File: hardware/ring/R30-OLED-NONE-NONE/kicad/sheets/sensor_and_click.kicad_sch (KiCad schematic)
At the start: 0 parts

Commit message: feat(hardware): scaffold 30deg optical ring sensor/click and usb interfaces for accessibility pointing, ~$9 ring BOM
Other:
- note added: "Sensor and click interface scaffold: optical SPI, motion interrupt, and dome-click nets are locked here before the PAW3204 symbol and dome footprint land."
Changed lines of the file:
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@@
   (generator_version "0.1")
   (paper "A4")
+  (text "Sensor and click interface scaffold: optical SPI, motion interrupt, and dome-click nets are locked here before the PAW3204 symbol and dome footprint land."
+    (at 20.32 20.32 0)
+    (effects (font (size 1.27 1.27)))
+  )
+  (hierarchical_label "VREG_3V3"
+    (shape input)
+    (at 25.4 38.1 0)
+    (effects (font (size 1.27 1.27)))
+  )
+  (hierarchical_label "SENSOR_SCLK"
+    (shape input)
+    (at 25.4 45.72 0)
+    (effects (font (size 1.27 1.27)))
+  )
+  (hierarchical_label "SENSOR_NRESET"
+    (shape input)
+    (at 25.4 53.34 0)
+    (effects (font (size 1.27 1.27)))
+  )
+  (hierarchical_label "SENSOR_SDIO"
+    (shape bidirectional)
+    (at 187.96 38.1 180)
+    (effects (font (size 1.27 1.27)))
+  )
+  (hierarchical_label "SENSOR_MOTION_N"
+    (shape output)
+    (at 187.96 45.72 180)
+    (effects (font (size 1.27 1.27)))
+  )
+  (hierarchical_label "CLICK_PRIMARY_N"
+    (shape output)
+    (at 187.96 53.34 180)
+    (effects (font (size 1.27 1.27)))
+  )
   (sheet_instances
     (path "/" (page "1"))

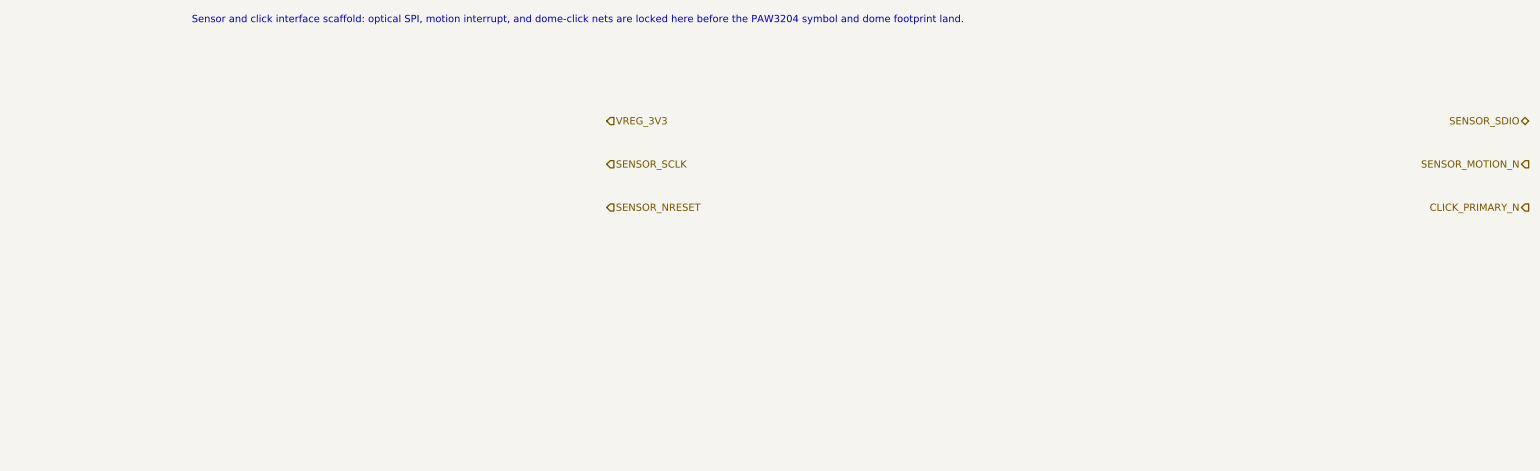
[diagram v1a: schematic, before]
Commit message: feat(hardware): lock R30 sense and schematic baseline
Design disclosure: sensing mechanism PAW3204-class optical tracking; form factor R30-OLED-NONE-NONE fingertip ring, active 30-degree ring packet; intended use BLE HID pointing for accessibility; BOM estimate ~$5.30-9.45.

Record the accepted 2N7002 charge-gate path, R7-R11 sense/status values, current KiCad red baseline, and directly linked packet truth docs.
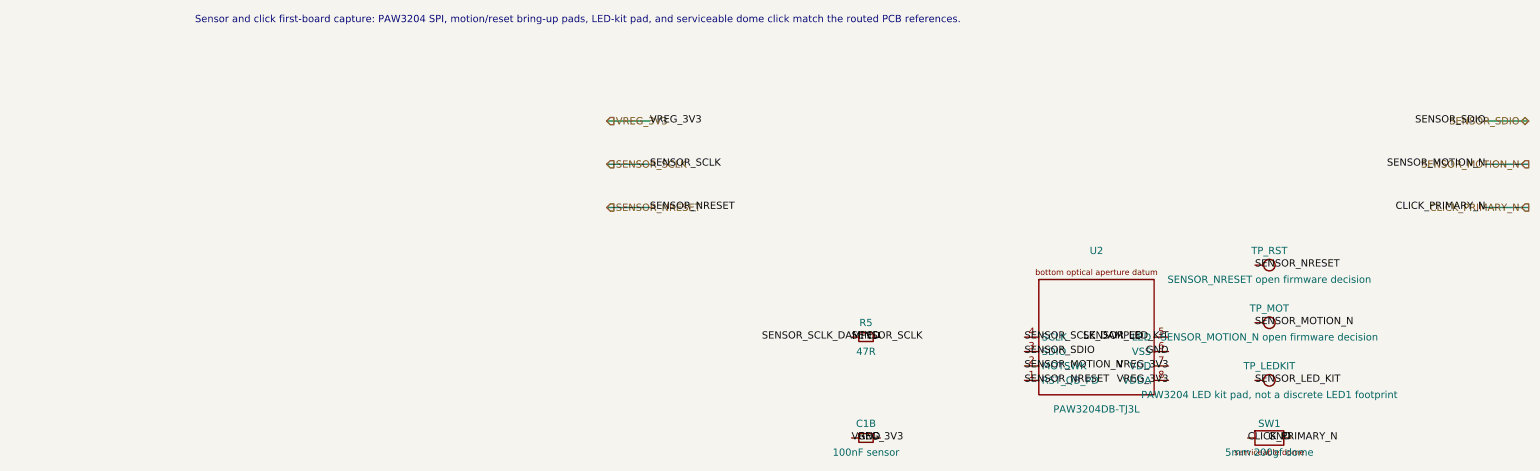
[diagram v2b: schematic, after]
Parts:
- added C1B: 100nF sensor, Capacitor_SMD:C_0402_1005Metric, symbol PowerFinger:C_0402_SUPPORT
- added R5: 47R, Resistor_SMD:R_0402_1005Metric, symbol PowerFinger:R_0402_SUPPORT
- added SW1: 5mm 200gf dome, PowerFinger_Ring:Snap_Dome_5mm_TwoPad_Serviceable, symbol PowerFinger:SNAP_DOME_2PAD
- added TP_LEDKIT: PAW3204 LED kit pad, not a discrete LED1 footprint, TestPoint:TestPoint_Pad_D1.0mm, symbol PowerFinger:TESTPAD_1MM
- added TP_MOT: SENSOR_MOTION_N open firmware decision, TestPoint:TestPoint_Pad_D1.0mm, symbol PowerFinger:TESTPAD_1MM
- added TP_RST: SENSOR_NRESET open firmware decision, TestPoint:TestPoint_Pad_D1.0mm, symbol PowerFinger:TESTPAD_1MM
- added U2: PAW3204DB-TJ3L, PowerFinger_Ring:PAW3204DB_TJ3L_Staggered_DIP8_Bottom_ApertureDatum, symbol PowerFinger:PAW3204DB-TJ3L_FirstBoard
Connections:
- net CLICK_PRIMARY_N: now also SW1.1 (CENTER)
- net SENSOR_MOTION_N: now also TP_MOT.1 (TP), U2.2 (MOTSWK)
- net SENSOR_NRESET: now also TP_RST.1 (TP), U2.1 (RST_QB_PD)
- net SENSOR_SCLK: now also R5.1
- net SENSOR_SDIO: now also U2.3 (SDIO)
- net VREG_3V3: now also C1B.1, U2.7 (VDD), U2.8 (VDDA)
- new net GND: C1B.2, SW1.2 (RING), U2.6 (VSS)
- new net SENSOR_LED_KIT: TP_LEDKIT.1 (TP), U2.5 (LED)
- new net SENSOR_SCLK_DAMPED: R5.2, U2.4 (SCLK)
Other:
- note added: "Sensor and click first-board capture: PAW3204 SPI, motion/reset bring-up pads, LED-kit pad, and serviceable dome click match the routed PCB references."
- note removed: "Sensor and click interface scaffold: optical SPI, motion interrupt, and dome-click nets are locked here before the PAW3204 symbol and dome footprint land."
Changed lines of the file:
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@@
   (generator_version "0.1")
   (paper "A4")
-  (text "Sensor and click interface scaffold: optical SPI, motion interrupt, and dome-click nets are locked here before the PAW3204 symbol and dome footprint land."
+  (text "Sensor and click first-board capture: PAW3204 SPI, motion/reset bring-up pads, LED-kit pad, and serviceable dome click match the routed PCB references."
     (at 20.32 20.32 0)
     (effects (font (size 1.27 1.27)))
   )
-  (hierarchical_label "VREG_3V3"
-    (shape input)
-    (at 25.4 38.1 0)
+  (hierarchical_label "VREG_3V3" (shape input) (at 25.4 38.1 0)
     (effects (font (size 1.27 1.27)))
   )
-  (hierarchical_label "SENSOR_SCLK"
-    (shape input)
-    (at 25.4 45.72 0)
+  (hierarchical_label "SENSOR_SCLK" (shape input) (at 25.4 45.72 0)
     (effects (font (size 1.27 1.27)))
   )
-  (hierarchical_label "SENSOR_NRESET"
-    (shape input)
-    (at 25.4 53.34 0)
+  (hierarchical_label "SENSOR_NRESET" (shape input) (at 25.4 53.34 0)
     (effects (font (size 1.27 1.27)))
   )
-  (hierarchical_label "SENSOR_SDIO"
-    (shape bidirectional)
-    (at 187.96 38.1 180)
+  (hierarchical_label "SENSOR_SDIO" (shape bidirectional) (at 187.96 38.1 180)
     (effects (font (size 1.27 1.27)))
   )
-  (hierarchical_label "SENSOR_MOTION_N"
-    (shape output)
-    (at 187.96 45.72 180)
+  (hierarchical_label "SENSOR_MOTION_N" (shape output) (at 187.96 45.72 180)
     (effects (font (size 1.27 1.27)))
   )
-  (hierarchical_label "CLICK_PRIMARY_N"
-    (shape output)
-    (at 187.96 53.34 180)
+  (hierarchical_label "CLICK_PRIMARY_N" (shape output) (at 187.96 53.34 180)
     (effects (font (size 1.27 1.27)))
   )
+  (wire (pts (xy 25.4 38.1) (xy 33.02 38.1)) (stroke (width 0) (type default) (color 0 0 0 0)))
+  (wire (pts (xy 25.4 45.72) (xy 33.02 45.72)) (stroke (width 0) (type default) (color 0 0 0 0)))
+  (wire (pts (xy 25.4 53.34) (xy 33.02 53.34)) (stroke (width 0) (type default) (color 0 0 0 0)))
+  (wire (pts (xy 180.34 38.1) (xy 187.96 38.1)) (stroke (width 0) (type default) (color 0 0 0 0)))
+  (wire (pts (xy 180.34 45.72) (xy 187.96 45.72)) (stroke (width 0) (type default) (color 0 0 0 0)))
+  (wire (pts (xy 180.34 53.34) (xy 187.96 53.34)) (stroke (width 0) (type default) (color 0 0 0 0)))
+  (label "VREG_3V3" (at 33.02 38.1 0) (effects (font (size 1.27 1.27))))
+  (label "SENSOR_SCLK" (at 33.02 45.72 0) (effects (font (size 1.27 1.27))))
+  (label "SENSOR_NRESET" (at 33.02 53.34 0) (effects (font (size 1.27 1.27))))
+  (label "SENSOR_SDIO" (at 180.34 38.1 180) (effects (font (size 1.27 1.27))))
+  (label "SENSOR_MOTION_N" (at 180.34 45.72 180) (effects (font (size 1.27 1.27))))
+  (label "CLICK_PRIMARY_N" (at 180.34 53.34 180) (effects (font (size 1.27 1.27))))
+  (symbol (lib_id "PowerFinger:PAW3204DB-TJ3L_FirstBoard") (at 111.76 76.2 0) (unit 1)
+    (in_bom yes) (on_board yes) (dnp no)
+    (property "Reference" "U2" (at 111.76 60.96 0)
+      (effects (font (size 1.27 1.27)))
+    )
+    (property "Value" "PAW3204DB-TJ3L" (at 111.76 88.9 0)
+      (effects (font (size 1.27 1.27)))
+    )
+    (property "Footprint" "PowerFinger_Ring:PAW3204DB_TJ3L_Staggered_DIP8_Bottom_ApertureDatum" (at 111.76 91.44 0)
+      (effects (font (size 1.27 1.27)) hide)
+    )
+    (property "Datasheet" "" (at 111.76 93.98 0)
+      (effects (font (size 1.27 1.27)) hide)
+    )
+    (pin "1")
+    (pin "2")
+    (pin "3")
+    (pin "4")
+    (pin "5")
+    (pin "6")
+    (pin "7")
+    (pin "8")
+    (instances
+      (project "r30_oled_none_none"
+        (path "/" (reference "U2") (unit 1))
+      )
+    )
+  )
+  (symbol (lib_id "PowerFinger:R_0402_SUPPORT") (at 71.12 76.2 0) (unit 1)
+    (in_bom yes) (on_board yes) (dnp no)
+    (property "Reference" "R5" (at 71.12 73.66 0)
+      (effects (font (size 1.27 1.27)))
+    )
+    (property "Value" "47R" (at 71.12 78.74 0)
+      (effects (font (size 1.27 1.27)))
+    )
+    (property "Footprint" "Resistor_SMD:R_0402_1005Metric" (at 71.12 81.28 0)
+      (effects (font (size 1.27 1.27)) hide)
+    )
+    (pin "1")
+    (pin "2")
+    (instances
+      (project "r30_oled_none_none"
+        (path "/" (reference "R5") (unit 1))
+      )
+    )
+  )
+  (symbol (lib_id "PowerFinger:C_0402_SUPPORT") (at 71.12 93.98 0) (unit 1)
+    (in_bom yes) (on_board yes) (dnp no)
+    (property "Reference" "C1B" (at 71.12 91.44 0)
+      (effects (font (size 1.27 1.27)))
+    )
+    (property "Value" "100nF sensor" (at 71.12 96.52 0)
+      (effects (font (size 1.27 1.27)))
+    )
+    (property "Footprint" "Capacitor_SMD:C_0402_1005Metric" (at 71.12 99.06 0)
+      (effects (font (size 1.27 1.27)) hide)
+    )
+    (property "Datasheet" "" (at 71.12 101.6 0)
+      (effects (font (size 1.27 1.27)) hide)
+    )
+    (pin "1")
+    (pin "2")
+    (instances
+      (project "r30_oled_none_none"
+        (path "/" (reference "C1B") (unit 1))
+      )
+    )
+  )
+  (symbol (lib_id "PowerFinger:SNAP_DOME_2PAD") (at 142.24 93.98 0) (unit 1)
+    (in_bom yes) (on_board yes) (dnp no)
+    (property "Reference" "SW1" (at 142.24 91.44 0)
+      (effects (font (size 1.27 1.27)))
+    )
+    (property "Value" "5mm 200gf dome" (at 142.24 96.52 0)
+      (effects (font (size 1.27 1.27)))
+    )
+    (property "Footprint" "PowerFinger_Ring:Snap_Dome_5mm_TwoPad_Serviceable" (at 142.24 99.06 0)
+      (effects (font (size 1.27 1.27)) hide)
+    )
+    (pin "1")
+    (pin "2")
+    (instances
+      (project "r30_oled_none_none"
+        (path "/" (reference "SW1") (unit 1))
+      )
+    )
+  )
+  (symbol (lib_id "PowerFinger:TESTPAD_1MM") (at 142.24 63.5 0) (unit 1)
+    (in_bom yes) (on_board yes) (dnp no)
+    (property "Reference" "TP_RST" (at 142.24 60.96 0)
+      (effects (font (size 1.27 1.27)))
+    )
+    (property "Value" "SENSOR_NRESET open firmware decision" (at 142.24 66.04 0)
+      (effects (font (size 1.27 1.27)))
+    )
+    (property "Footprint" "TestPoint:TestPoint_Pad_D1.0mm" (at 142.24 68.58 0)
+      (effects (font (size 1.27 1.27)) hide)
+    )
+    (pin "1")
+    (instances
+      (project "r30_oled_none_none"
+        (path "/" (reference "TP_RST") (unit 1))
+      )
+    )
+  )
+  (symbol (lib_id "PowerFinger:TESTPAD_1MM") (at 142.24 73.66 0) (unit 1)
+    (in_bom yes) (on_board yes) (dnp no)
+    (property "Reference" "TP_MOT" (at 142.24 71.12 0)
+      (effects (font (size 1.27 1.27)))
+    )
+    (property "Value" "SENSOR_MOTION_N open firmware decision" (at 142.24 76.2 0)
+      (effects (font (size 1.27 1.27)))
+    )
+    (property "Footprint" "TestPoint:TestPoint_Pad_D1.0mm" (at 142.24 78.74 0)
+      (effects (font (size 1.27 1.27)) hide)
+    )
+    (pin "1")
+    (instances
+      (project "r30_oled_none_none"
+        (path "/" (reference "TP_MOT") (unit 1))
+      )
+    )
+  )
+  (symbol (lib_id "PowerFinger:TESTPAD_1MM") (at 142.24 83.82 0) (unit 1)
+    (in_bom yes) (on_board yes) (dnp no)
+    (property "Reference" "TP_LEDKIT" (at 142.24 81.28 0)
+      (effects (font (size 1.27 1.27)))
+    )
+    (property "Value" "PAW3204 LED kit pad, not a discrete LED1 footprint" (at 142.24 86.36 0)
+      (effects (font (size 1.27 1.27)))
+    )
+    (property "Footprint" "TestPoint:TestPoint_Pad_D1.0mm" (at 142.24 88.9 0)
+      (effects (font (size 1.27 1.27)) hide)
+    )
+    (pin "1")
+    (instances
+      (project "r30_oled_none_none"
+        (path "/" (reference "TP_LEDKIT") (unit 1))
+      )
+    )
+  )
+  (label "SENSOR_NRESET" (at 99.06 83.82 0) (effects (font (size 1.27 1.27))))
+  (label "SENSOR_MOTION_N" (at 99.06 81.28 0) (effects (font (size 1.27 1.27))))
+  (label "SENSOR_SDIO" (at 99.06 78.74 0) (effects (font (size 1.27 1.27))))
+  (label "SENSOR_SCLK_DAMPED" (at 99.06 76.2 0) (effects (font (size 1.27 1.27))))
+  (label "SENSOR_LED_KIT" (at 124.46 76.2 180) (effects (font (size 1.27 1.27))))
+  (label "GND" (at 124.46 78.74 180) (effects (font (size 1.27 1.27))))
+  (label "VREG_3V3" (at 124.46 81.28 180) (effects (font (size 1.27 1.27))))
+  (label "VREG_3V3" (at 124.46 83.82 180) (effects (font (size 1.27 1.27))))
+  (label "SENSOR_SCLK" (at 68.58 76.2 0) (effects (font (size 1.27 1.27))))
+  (label "SENSOR_SCLK_DAMPED" (at 73.66 76.2 180) (effects (font (size 1.27 1.27))))
+  (label "VREG_3V3" (at 68.58 93.98 0) (effects (font (size 1.27 1.27))))
+  (label "GND" (at 73.66 93.98 180) (effects (font (size 1.27 1.27))))
+  (label "CLICK_PRIMARY_N" (at 138.43 93.98 0) (effects (font (size 1.27 1.27))))
+  (label "GND" (at 146.05 93.98 180) (effects (font (size 1.27 1.27))))
+  (label "SENSOR_NRESET" (at 139.7 63.5 0) (effects (font (size 1.27 1.27))))
+  (label "SENSOR_MOTION_N" (at 139.7 73.66 0) (effects (font (size 1.27 1.27))))
+  (label "SENSOR_LED_KIT" (at 139.7 83.82 0) (effects (font (size 1.27 1.27))))
   (sheet_instances
     (path "/" (page "1"))

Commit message: fix(r30): clean schematic erc library baseline
Design disclosure: sensing mechanism PAW3204-class optical tracking; form factor R30-OLED-NONE-NONE fingertip ring, active 30-degree ring packet; intended use BLE HID pointing for accessibility; BOM estimate ~$5.30-9.45.

Materialize the project-local PowerFinger symbol and PowerFinger_Ring footprint libraries, wire sheet-interface labels, keep PAW3204 reset/motion local to sensor test pads, and update the verified KiCad snapshot to ERC=0, DRC=349, unconnected=41, parity=118.
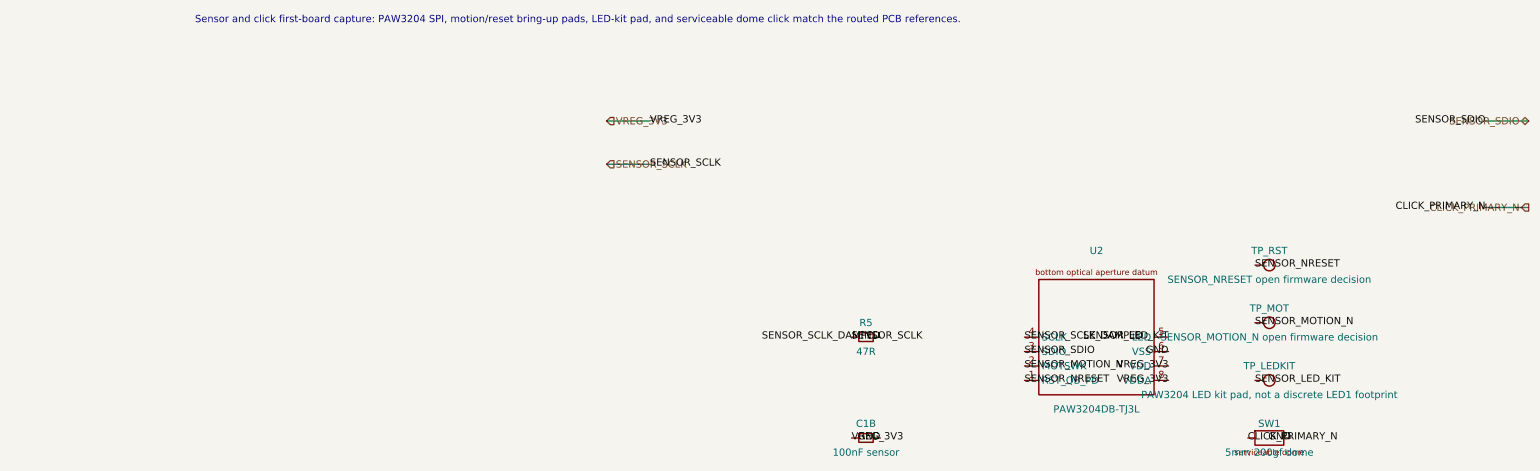
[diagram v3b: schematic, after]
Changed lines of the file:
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@@
     (effects (font (size 1.27 1.27)))
   )
-  (hierarchical_label "SENSOR_NRESET" (shape input) (at 25.4 53.34 0)
+    (hierarchical_label "SENSOR_SDIO" (shape bidirectional) (at 187.96 38.1 180)
     (effects (font (size 1.27 1.27)))
   )
-  (hierarchical_label "SENSOR_SDIO" (shape bidirectional) (at 187.96 38.1 180)
-    (effects (font (size 1.27 1.27)))
-  )
-  (hierarchical_label "SENSOR_MOTION_N" (shape output) (at 187.96 45.72 180)
-    (effects (font (size 1.27 1.27)))
-  )
-  (hierarchical_label "CLICK_PRIMARY_N" (shape output) (at 187.96 53.34 180)
+    (hierarchical_label "CLICK_PRIMARY_N" (shape output) (at 187.96 53.34 180)
     (effects (font (size 1.27 1.27)))
   )
   (wire (pts (xy 25.4 38.1) (xy 33.02 38.1)) (stroke (width 0) (type default) (color 0 0 0 0)))
   (wire (pts (xy 25.4 45.72) (xy 33.02 45.72)) (stroke (width 0) (type default) (color 0 0 0 0)))
-  (wire (pts (xy 25.4 53.34) (xy 33.02 53.34)) (stroke (width 0) (type default) (color 0 0 0 0)))
-  (wire (pts (xy 180.34 38.1) (xy 187.96 38.1)) (stroke (width 0) (type default) (color 0 0 0 0)))
-  (wire (pts (xy 180.34 45.72) (xy 187.96 45.72)) (stroke (width 0) (type default) (color 0 0 0 0)))
-  (wire (pts (xy 180.34 53.34) (xy 187.96 53.34)) (stroke (width 0) (type default) (color 0 0 0 0)))
+    (wire (pts (xy 180.34 38.1) (xy 187.96 38.1)) (stroke (width 0) (type default) (color 0 0 0 0)))
+    (wire (pts (xy 180.34 53.34) (xy 187.96 53.34)) (stroke (width 0) (type default) (color 0 0 0 0)))
   (label "VREG_3V3" (at 33.02 38.1 0) (effects (font (size 1.27 1.27))))
   (label "SENSOR_SCLK" (at 33.02 45.72 0) (effects (font (size 1.27 1.27))))
-  (label "SENSOR_NRESET" (at 33.02 53.34 0) (effects (font (size 1.27 1.27))))
-  (label "SENSOR_SDIO" (at 180.34 38.1 180) (effects (font (size 1.27 1.27))))
-  (label "SENSOR_MOTION_N" (at 180.34 45.72 180) (effects (font (size 1.27 1.27))))
-  (label "CLICK_PRIMARY_N" (at 180.34 53.34 180) (effects (font (size 1.27 1.27))))
+    (label "SENSOR_SDIO" (at 180.34 38.1 180) (effects (font (size 1.27 1.27))))
+    (label "CLICK_PRIMARY_N" (at 180.34 53.34 180) (effects (font (size 1.27 1.27))))
   (symbol (lib_id "PowerFinger:PAW3204DB-TJ3L_FirstBoard") (at 111.76 76.2 0) (unit 1)
     (in_bom yes) (on_board yes) (dnp no)
